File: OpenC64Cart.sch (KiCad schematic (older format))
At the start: 17 parts, among them J99 PEG_HOLE, SW1 RESET_SW, SW101 SW_Coded_SH-7010, U1 C64-Exp-Port, U101 74LS02, U102 4066, U2 27512

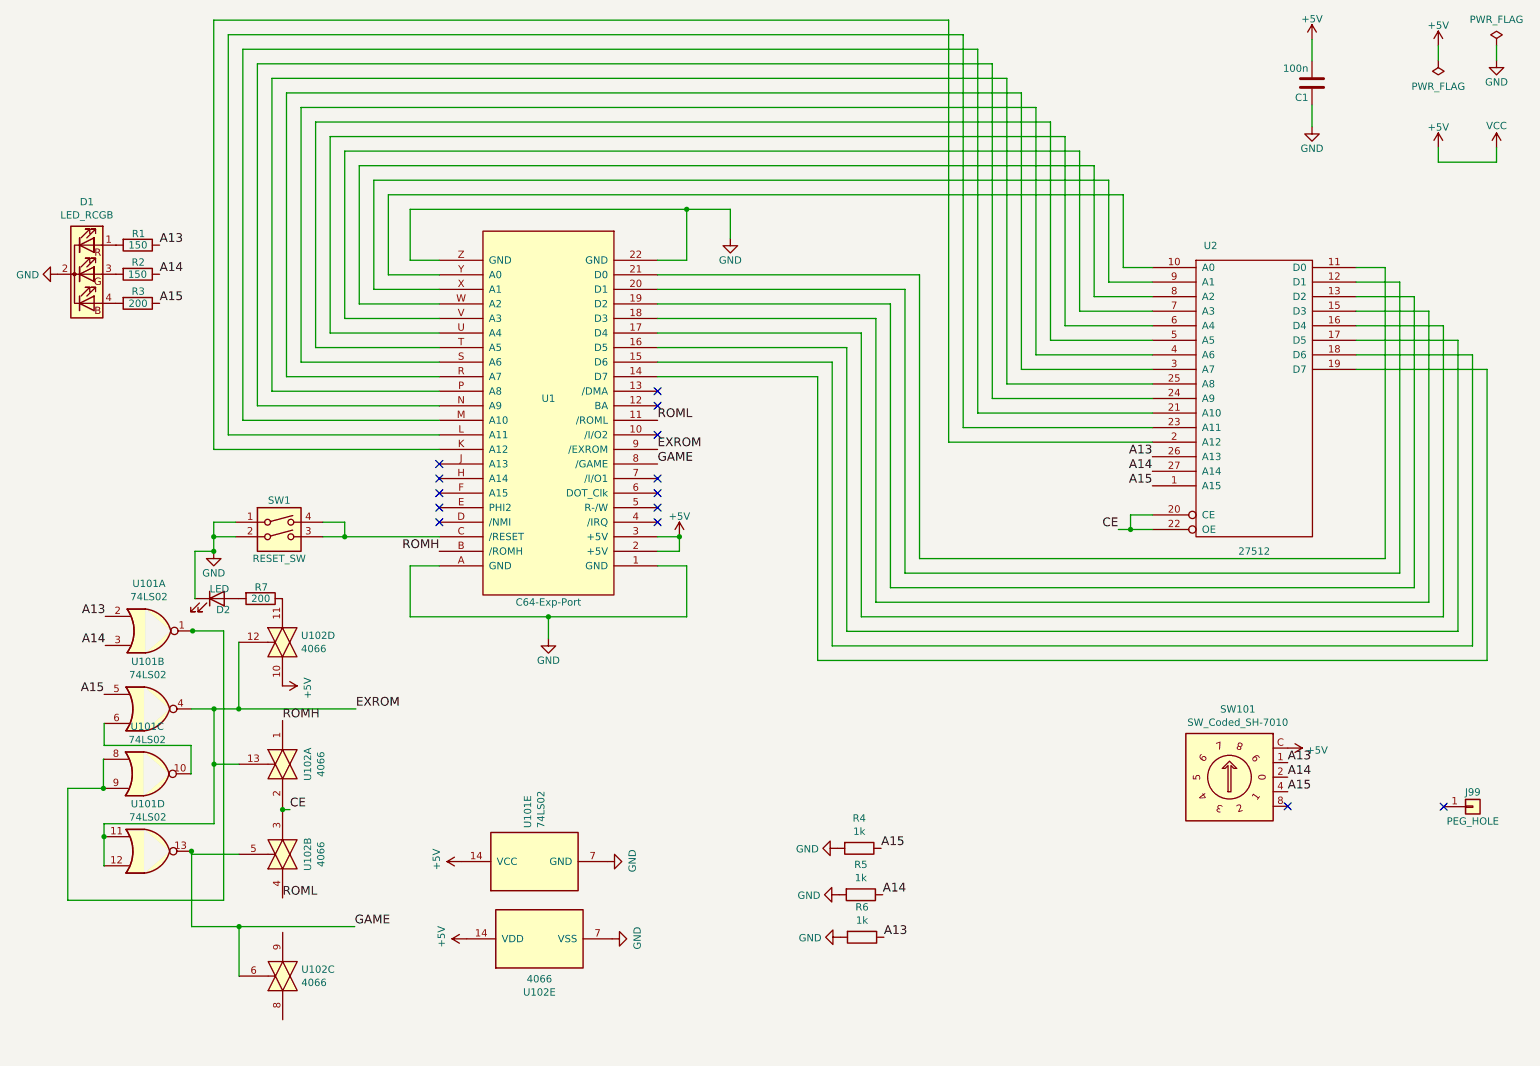
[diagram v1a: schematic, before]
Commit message: Tested
Finally received the latest revision PCB and everything is now working. I tweaked the LED resistors for the RGB LEDs I have but they may need tweaked depending on the actual specs of the LED used.
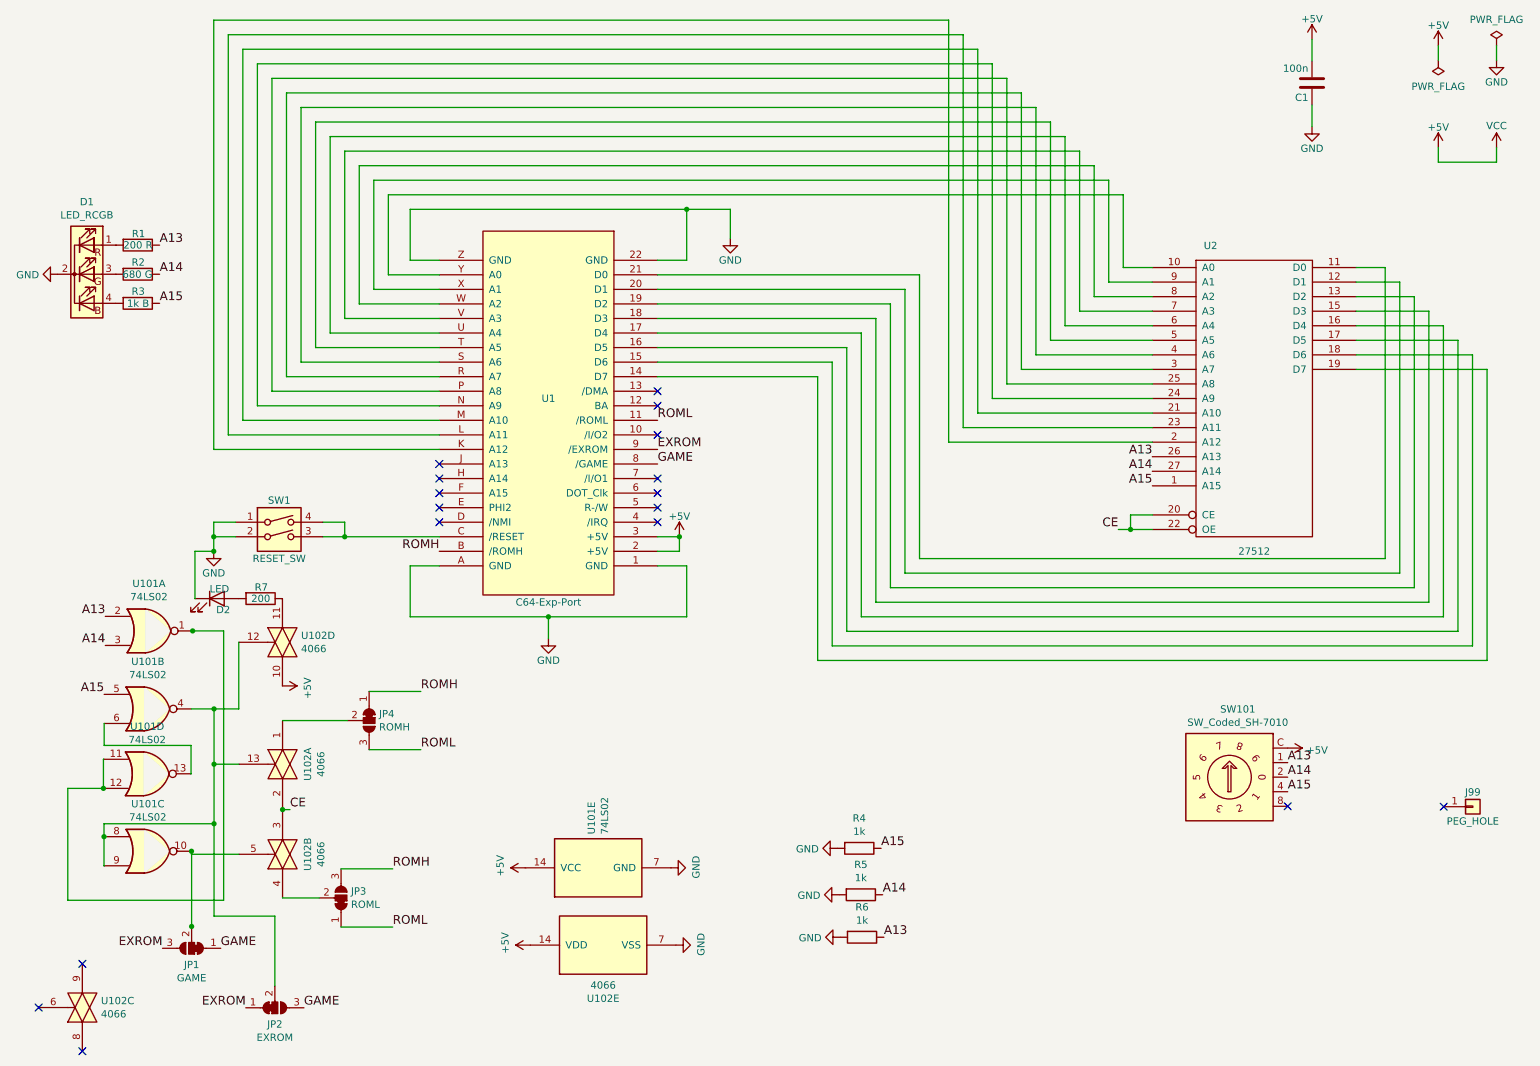
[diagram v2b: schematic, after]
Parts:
- added JP1: GAME, Jumper:SolderJumper-3_P1.3mm_Bridged12_RoundedPad1.0x1.5mm_NumberLabels, symbol Jumper:SolderJumper_3_Bridged12
- added JP2: EXROM, Jumper:SolderJumper-3_P1.3mm_Bridged12_RoundedPad1.0x1.5mm_NumberLabels, symbol Jumper:SolderJumper_3_Bridged12
- added JP3: ROML, Jumper:SolderJumper-3_P1.3mm_Bridged12_RoundedPad1.0x1.5mm_NumberLabels, symbol Jumper:SolderJumper_3_Bridged12
- added JP4: ROMH, Jumper:SolderJumper-3_P1.3mm_Bridged12_RoundedPad1.0x1.5mm_NumberLabels, symbol Jumper:SolderJumper_3_Bridged12
- R1: value 150 -> 200 R
- R2: value 150 -> 680 G
- R3: value 200 -> 1k B
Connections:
- net EXROM: now also JP1.3 (B), JP2.1 (A); no longer U101.11, U101.12, U101.4, U102.12, U102.13
- net GAME: now also JP1.1 (A), JP2.3 (B); no longer U101.13, U102.5, U102.6
- net ROMH: now also JP3.3 (B), JP4.1 (A); no longer U102.1
- net ROML: now also JP3.1 (A), JP4.3 (B); no longer U102.4
- net at U101.8, U101.9: now also U101.4, U102.12, U102.13, JP2.2 (C); no longer U101.1
- net at U101.6: now also U101.13; no longer U101.10
- new net: U101.1, U101.11, U101.12
- new net: JP1.2 (C), U101.10, U102.5
- new net: JP4.2 (C), U102.1
- new net: JP3.2 (C), U102.4
- no-connect marks 14 -> 17
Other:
- moved on the sheet: U101C, U101D, U101E, U102C, U102E
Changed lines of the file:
@@
 L 74xx:74LS02 U101
 U 5 1 61921332
-P 4285 6422
-F 0 "U101" H 4515 6468 50  0000 L CNN
-F 1 "74LS02" H 4515 6377 50  0000 L CNN
-F 2 "Package_DIP:DIP-14_W7.62mm" H 4285 6422 50  0001 C CNN
-F 3 "http://www.ti.com/lit/gpn/sn74ls02" H 4285 6422 50  0001 C CNN
-	5    4285 6422
+P 4723 6465
+F 0 "U101" H 4953 6511 50  0000 L CNN
+F 1 "74LS02" H 4953 6420 50  0000 L CNN
+F 2 "Package_DIP:DIP-14_W7.62mm" H 4723 6465 50  0001 C CNN
+F 3 "http://www.ti.com/lit/gpn/sn74ls02" H 4723 6465 50  0001 C CNN
+	5    4723 6465
 	0    -1   -1   0
 $EndComp
@@
 L 74xx:74LS02 U101
 U 4 1 6191F59C
+P 1624 5819
+F 0 "U101" H 1624 6144 50  0000 C CNN
+F 1 "74LS02" H 1624 6053 50  0000 C CNN
+F 2 "Package_DIP:DIP-14_W7.62mm" H 1624 5819 50  0001 C CNN
+F 3 "http://www.ti.com/lit/gpn/sn74ls02" H 1624 5819 50  0001 C CNN
+	4    1624 5819
+	1    0    0    -1
+$EndComp
+$Comp
+L 74xx:74LS02 U101
+U 3 1 6191CC05
 P 1628 6351
 F 0 "U101" H 1628 6676 50  0000 C CNN
@@
 F 2 "Package_DIP:DIP-14_W7.62mm" H 1628 6351 50  0001 C CNN
 F 3 "http://www.ti.com/lit/gpn/sn74ls02" H 1628 6351 50  0001 C CNN
-	4    1628 6351
-	1    0    0    -1
-$EndComp
-$Comp
-L 74xx:74LS02 U101
-U 3 1 6191CC05
-P 1624 5819
-F 0 "U101" H 1624 6144 50  0000 C CNN
-F 1 "74LS02" H 1624 6053 50  0000 C CNN
-F 2 "Package_DIP:DIP-14_W7.62mm" H 1624 5819 50  0001 C CNN
-F 3 "http://www.ti.com/lit/gpn/sn74ls02" H 1624 5819 50  0001 C CNN
-	3    1624 5819
+	3    1628 6351
 	1    0    0    -1
 $EndComp
@@
 L power:GND #PWR0101
 U 1 1 6191FDAD
-P 4785 6422
-F 0 "#PWR0101" H 4785 6172 50  0001 C CNN
-F 1 "GND" H 4790 6249 50  0000 C CNN
-F 2 "" H 4785 6422 50  0001 C CNN
-F 3 "" H 4785 6422 50  0001 C CNN
-	1    4785 6422
+P 5223 6465
+F 0 "#PWR0101" H 5223 6215 50  0001 C CNN
+F 1 "GND" H 5228 6292 50  0000 C CNN
+F 2 "" H 5223 6465 50  0001 C CNN
+F 3 "" H 5223 6465 50  0001 C CNN
+	1    5223 6465
 	0    -1   -1   0
 $EndComp
@@
 L power:+5V #PWR0102
 U 1 1 61920AEE
-P 3785 6422
-F 0 "#PWR0102" H 3785 6272 50  0001 C CNN
-F 1 "+5V" H 3800 6595 50  0000 C CNN
-F 2 "" H 3785 6422 50  0001 C CNN
-F 3 "" H 3785 6422 50  0001 C CNN
-	1    3785 6422
+P 4223 6465
+F 0 "#PWR0102" H 4223 6315 50  0001 C CNN
+F 1 "+5V" H 4238 6638 50  0000 C CNN
+F 2 "" H 4223 6465 50  0001 C CNN
+F 3 "" H 4223 6465 50  0001 C CNN
+	1    4223 6465
 	0    -1   -1   0
 $EndComp
@@
 	1924 5819 1925 5819
 Wire Wire Line
-	1925 5819 1925 5624
-Wire Wire Line
 	1925 5624 1328 5624
 Wire Wire Line
@@
 Wire Wire Line
 	1327 6162 2083 6162
-Wire Wire Line
-	2083 6162 2083 5753
 Connection ~ 2083 5753
 Wire Wire Line
@@
 Connection ~ 2083 5373
 Wire Wire Line
-	3050 6869 2255 6869
-Wire Wire Line
 	1929 6351 1928 6351
 $Comp
 L power:GND #PWR0107
 U 1 1 61C27FBE
-P 4819 6953
-F 0 "#PWR0107" H 4819 6703 50  0001 C CNN
-F 1 "GND" H 4824 6780 50  0000 C CNN
-F 2 "" H 4819 6953 50  0001 C CNN
-F 3 "" H 4819 6953 50  0001 C CNN
-	1    4819 6953
+P 5257 6996
+F 0 "#PWR0107" H 5257 6746 50  0001 C CNN
+F 1 "GND" H 5262 6823 50  0000 C CNN
+F 2 "" H 5257 6996 50  0001 C CNN
+F 3 "" H 5257 6996 50  0001 C CNN
+	1    5257 6996
 	0    -1   -1   0
 $EndComp
@@
 L power:+5V #PWR0108
 U 1 1 61C32C24
-P 3819 6953
-F 0 "#PWR0108" H 3819 6803 50  0001 C CNN
-F 1 "+5V" H 3834 7126 50  0000 C CNN
-F 2 "" H 3819 6953 50  0001 C CNN
-F 3 "" H 3819 6953 50  0001 C CNN
-	1    3819 6953
+P 4257 6996
+F 0 "#PWR0108" H 4257 6846 50  0001 C CNN
+F 1 "+5V" H 4272 7169 50  0000 C CNN
+F 2 "" H 4257 6996 50  0001 C CNN
+F 3 "" H 4257 6996 50  0001 C CNN
+	1    4257 6996
 	0    -1   -1   0
 $EndComp
@@
 P 1559 2586
 F 0 "R3" V 1477 2589 50  0000 C CNN
-F 1 "200" V 1560 2588 50  0000 C CNN
+F 1 "1k B" V 1560 2588 50  0000 C CNN
 F 2 "Resistor_THT:R_Axial_DIN0207_L6.3mm_D2.5mm_P7.62mm_Horizontal" V 1489 2586 50  0001 C CNN
 F 3 "~" H 1559 2586 50  0001 C CNN
@@
 P 1559 2186
 F 0 "R1" V 1481 2191 50  0000 C CNN
-F 1 "150" V 1559 2187 50  0000 C CNN
+F 1 "200 R" V 1559 2187 50  0000 C CNN
 F 2 "Resistor_THT:R_Axial_DIN0207_L6.3mm_D2.5mm_P7.62mm_Horizontal" V 1489 2186 50  0001 C CNN
 F 3 "~" H 1559 2186 50  0001 C CNN
@@
 P 1559 2386
 F 0 "R2" V 1477 2389 50  0000 C CNN
-F 1 "150" V 1560 2384 50  0000 C CNN
+F 1 "680 G" V 1560 2384 50  0000 C CNN
 F 2 "Resistor_THT:R_Axial_DIN0207_L6.3mm_D2.5mm_P7.62mm_Horizontal" V 1489 2386 50  0001 C CNN
 F 3 "~" H 1559 2386 50  0001 C CNN
@@
 	1    6367 6331
 	0    1    1    0
-$EndComp
-$Comp
-L 4xxx:4066 U102
-U 3 1 61AF60DC
-P 2555 7209
-F 0 "U102" V 2601 7081 50  0000 R CNN
-F 1 "4066" V 2510 7081 50  0000 R CNN
-F 2 "Package_DIP:DIP-14_W7.62mm" H 2555 7209 50  0001 C CNN
-F 3 "http://www.ti.com/lit/ds/symlink/cd4066b.pdf" H 2555 7209 50  0001 C CNN
-	3    2555 7209
-	0    -1   -1   0
 $EndComp
 $Comp
@@
 $EndComp
 Wire Wire Line
-	2255 7209 2255 6869
-Connection ~ 2255 6869
-Wire Wire Line
-	2255 6869 1929 6869
-Wire Wire Line
 	2253 4915 2253 5373
 $Comp
@@
 L 4xxx:4066 U102
 U 5 1 61C253FE
-P 4319 6953
-F 0 "U102" V 3952 6953 50  0000 C CNN
-F 1 "4066" V 4043 6953 50  0000 C CNN
-F 2 "Package_DIP:DIP-14_W7.62mm" H 4319 6953 50  0001 C CNN
-F 3 "http://www.ti.com/lit/ds/symlink/cd4066b.pdf" H 4319 6953 50  0001 C CNN
-	5    4319 6953
+P 4757 6996
+F 0 "U102" V 4390 6996 50  0000 C CNN
+F 1 "4066" V 4481 6996 50  0000 C CNN
+F 2 "Package_DIP:DIP-14_W7.62mm" H 4757 6996 50  0001 C CNN
+F 3 "http://www.ti.com/lit/ds/symlink/cd4066b.pdf" H 4757 6996 50  0001 C CNN
+	5    4757 6996
 	0    -1   -1   0
 $EndComp
@@
 Wire Wire Line
 	2083 5373 2253 5373
-Connection ~ 2253 5373
-Wire Wire Line
-	2253 5373 3058 5373
 Wire Wire Line
 	1929 4837 1936 4837
@@
 Wire Wire Line
 	1936 4837 2149 4837
-Text Label 2554 6672 0    60   ~ 0
-ROML
-Text Label 2554 5453 0    60   ~ 0
-ROMH
-Text Label 3050 6869 0    60   ~ 0
-GAME
-Text Label 3058 5373 0    60   ~ 0
+Text Label 1729 7018 2    60   ~ 0
 EXROM
-Wire Wire Line
-	1929 6351 1929 6869
+Text Label 2301 7427 2    60   ~ 0
+EXROM
 Wire Wire Line
 	1928 6372 1928 6351
@@
 Wire Wire Line
 	8381 4140 8531 4140
+Wire Wire Line
+	1925 5624 1925 5819
+$Comp
+L Jumper:SolderJumper_3_Bridged12 JP2
+U 1 1 61BB626C
+P 2501 7427
+F 0 "JP2" H 2501 7540 50  0000 C CNN
+F 1 "EXROM" H 2501 7631 50  0000 C CNN
+F 2 "Jumper:SolderJumper-3_P1.3mm_Bridged12_RoundedPad1.0x1.5mm_NumberLabels" H 2501 7427 50  0001 C CNN
+F 3 "~" H 2501 7427 50  0001 C CNN
+	1    2501 7427
+	1    0    0    1
+$EndComp
+Text Label 2701 7427 0    60   ~ 0
+GAME
+$Comp
+L 4xxx:4066 U102
+U 3 1 61AF60DC
+P 1178 7425
+F 0 "U102" V 1224 7297 50  0000 R CNN
+F 1 "4066" V 1133 7297 50  0000 R CNN
+F 2 "Package_DIP:DIP-14_W7.62mm" H 1178 7425 50  0001 C CNN
+F 3 "http://www.ti.com/lit/ds/symlink/cd4066b.pdf" H 1178 7425 50  0001 C CNN
+	3    1178 7425
+	0    -1   -1   0
+$EndComp
+Wire Wire Line
+	1929 6351 1929 6868
+Connection ~ 1929 6868
+Wire Wire Line
+	1929 6868 1929 6869
+Wire Wire Line
+	2083 6797 2501 6797
+Wire Wire Line
+	2501 6797 2501 7277
+Wire Wire Line
+	2083 5753 2083 6162
+Connection ~ 2083 6162
+Wire Wire Line
+	2083 6162 2083 6797
+$Comp
+L Jumper:SolderJumper_3_Bridged12 JP4
+U 1 1 61BDC9B0
+P 3149 5453
+F 0 "JP4" V 3103 5521 50  0000 L CNN
+F 1 "ROMH" V 3194 5521 50  0000 L CNN
+F 2 "Jumper:SolderJumper-3_P1.3mm_Bridged12_RoundedPad1.0x1.5mm_NumberLabels" H 3149 5453 50  0001 C CNN
+F 3 "~" H 3149 5453 50  0001 C CNN
+	1    3149 5453
+	0    1    1    0
+$EndComp
+Text Label 3504 5653 0    60   ~ 0
+ROML
+Wire Wire Line
+	2554 5453 2999 5453
+Wire Wire Line
+	3149 5653 3504 5653
+Text Label 3504 5253 0    60   ~ 0
+ROMH
+Wire Wire Line
+	3149 5253 3504 5253
+Wire Wire Line
+	2956 6872 3311 6872
+Wire Wire Line
+	2956 6472 3311 6472
+NoConn ~ 1178 7725
+NoConn ~ 878  7425
+NoConn ~ 1178 7125
+Text Label 2129 7018 0    60   ~ 0
+GAME
+Text Label 3311 6872 0    60   ~ 0
+ROML
+Text Label 3311 6472 0    60   ~ 0
+ROMH
+Wire Wire Line
+	2554 6672 2806 6672
+$Comp
+L Jumper:SolderJumper_3_Bridged12 JP3
+U 1 1 61D6897E
+P 2956 6672
+F 0 "JP3" V 3002 6740 50  0000 L CNN
+F 1 "ROML" V 2911 6740 50  0000 L CNN
+F 2 "Jumper:SolderJumper-3_P1.3mm_Bridged12_RoundedPad1.0x1.5mm_NumberLabels" H 2956 6672 50  0001 C CNN
+F 3 "~" H 2956 6672 50  0001 C CNN
+	1    2956 6672
+	0    1    -1   0
+$EndComp
+$Comp
+L Jumper:SolderJumper_3_Bridged12 JP1
+U 1 1 61BB6F84
+P 1929 7018
+F 0 "JP1" H 1929 7131 50  0000 C CNN
+F 1 "GAME" H 1929 7222 50  0000 C CNN
+F 2 "Jumper:SolderJumper-3_P1.3mm_Bridged12_RoundedPad1.0x1.5mm_NumberLabels" H 1929 7018 50  0001 C CNN
+F 3 "~" H 1929 7018 50  0001 C CNN
+	1    1929 7018
+	-1   0    0    1
+$EndComp
 $EndSCHEMATC
